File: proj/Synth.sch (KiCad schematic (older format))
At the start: 53 parts, among them U3 LMH6714MF, U4 AD9958BCPZ, U5 LMH6714MF, X1 25 MHz

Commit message: Lots of layout work
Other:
- note added: "Differential T-line\nZdiff = 100, Z0 = 67\nSpecs for OSH Park 4L:\n0.1415 track, 0.1584 space (0.299 align)\nSpecs for Elecrow 4L:\n0.21 track, 0.16 space"
- note removed: "Differential T-line\nZdiff = 100, Z0 = 67\nSpecs for OSH Park 4L:\n0.1415 track, 0.1584 space (0.299 align)"

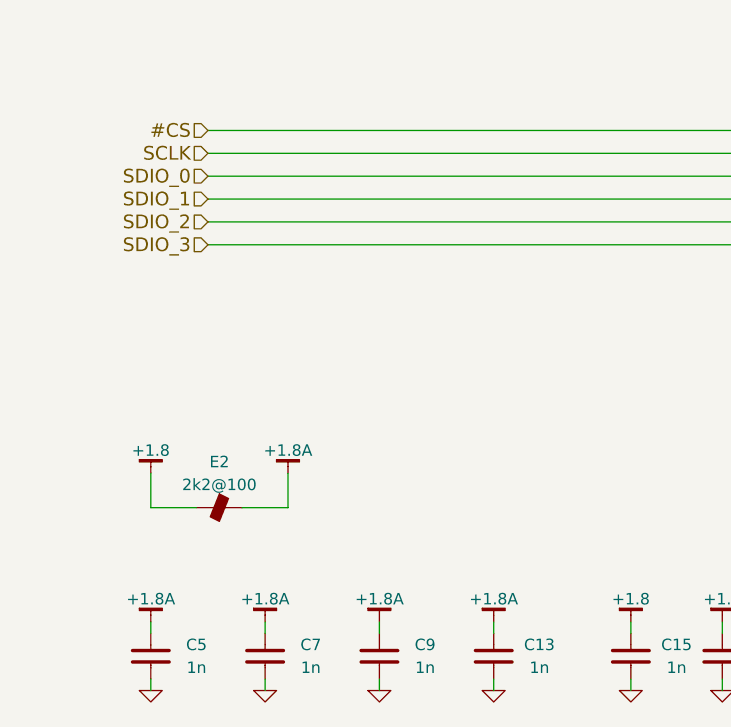
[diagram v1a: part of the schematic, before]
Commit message: All parts placed
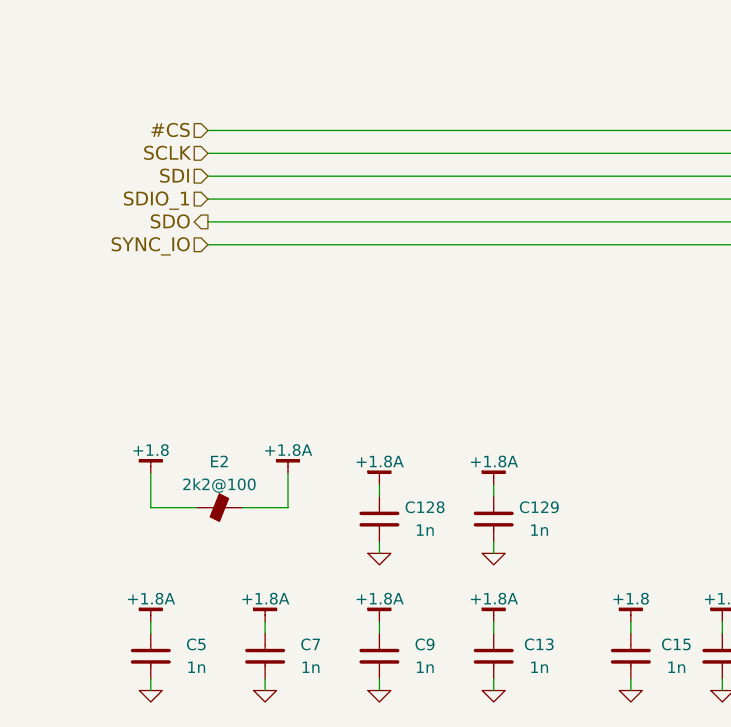
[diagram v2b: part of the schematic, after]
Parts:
- added C128, C129: 1n, IPC7351-Nominal:CAPC1005X55, symbol C-0402
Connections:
- net +1.8A: now also C128.1, C129.1
- net GND: now also C128.2, C129.2
- net SDIO_0 renamed SDI
- net SDIO_2 renamed SDO
- net SDIO_3 renamed SYNC_IO

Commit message: Some work removing unnecessary bits
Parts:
- removed R12, R16: 100, IPC7351-Nominal:RESC1005X40, symbol R-0402
- added R12: 0R, IPC7351-Nominal:RESC1608X50, symbol R-0603
- R31, R32: value 2k2 -> 1k91; BOM RES SMD 2.2k 5% [0402] -> RES SMD 1.91k 5% [0402]
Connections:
- net +1.8A: now also R12.2
- net GND: no longer C23.2
- net at U4.2 (SYNC_OUT): now also TP1.1
- net at U4.54 (SYNC_CLK): now also TP2.1
- new net: C23.2, R12.1
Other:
- note added: "@R12 is copper-bridged on the PCB, it is not necessary to populate a jumper.\nIf this part must be changed after testing, cut the bridge."
- moved on the sheet: TP1, TP2
